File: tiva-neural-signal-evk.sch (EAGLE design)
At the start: 88 parts, among them IC1 TM4C123G, IC2 TLV70233, IC3 INA2332, IC4 OPA2320, IC5 OPA2320, IC6 INA2332, IC7 OPA2320, IC8 OPA2320, X1 USB, X2 MICROSD, Y1 16MHz, Y2 32.768kHz

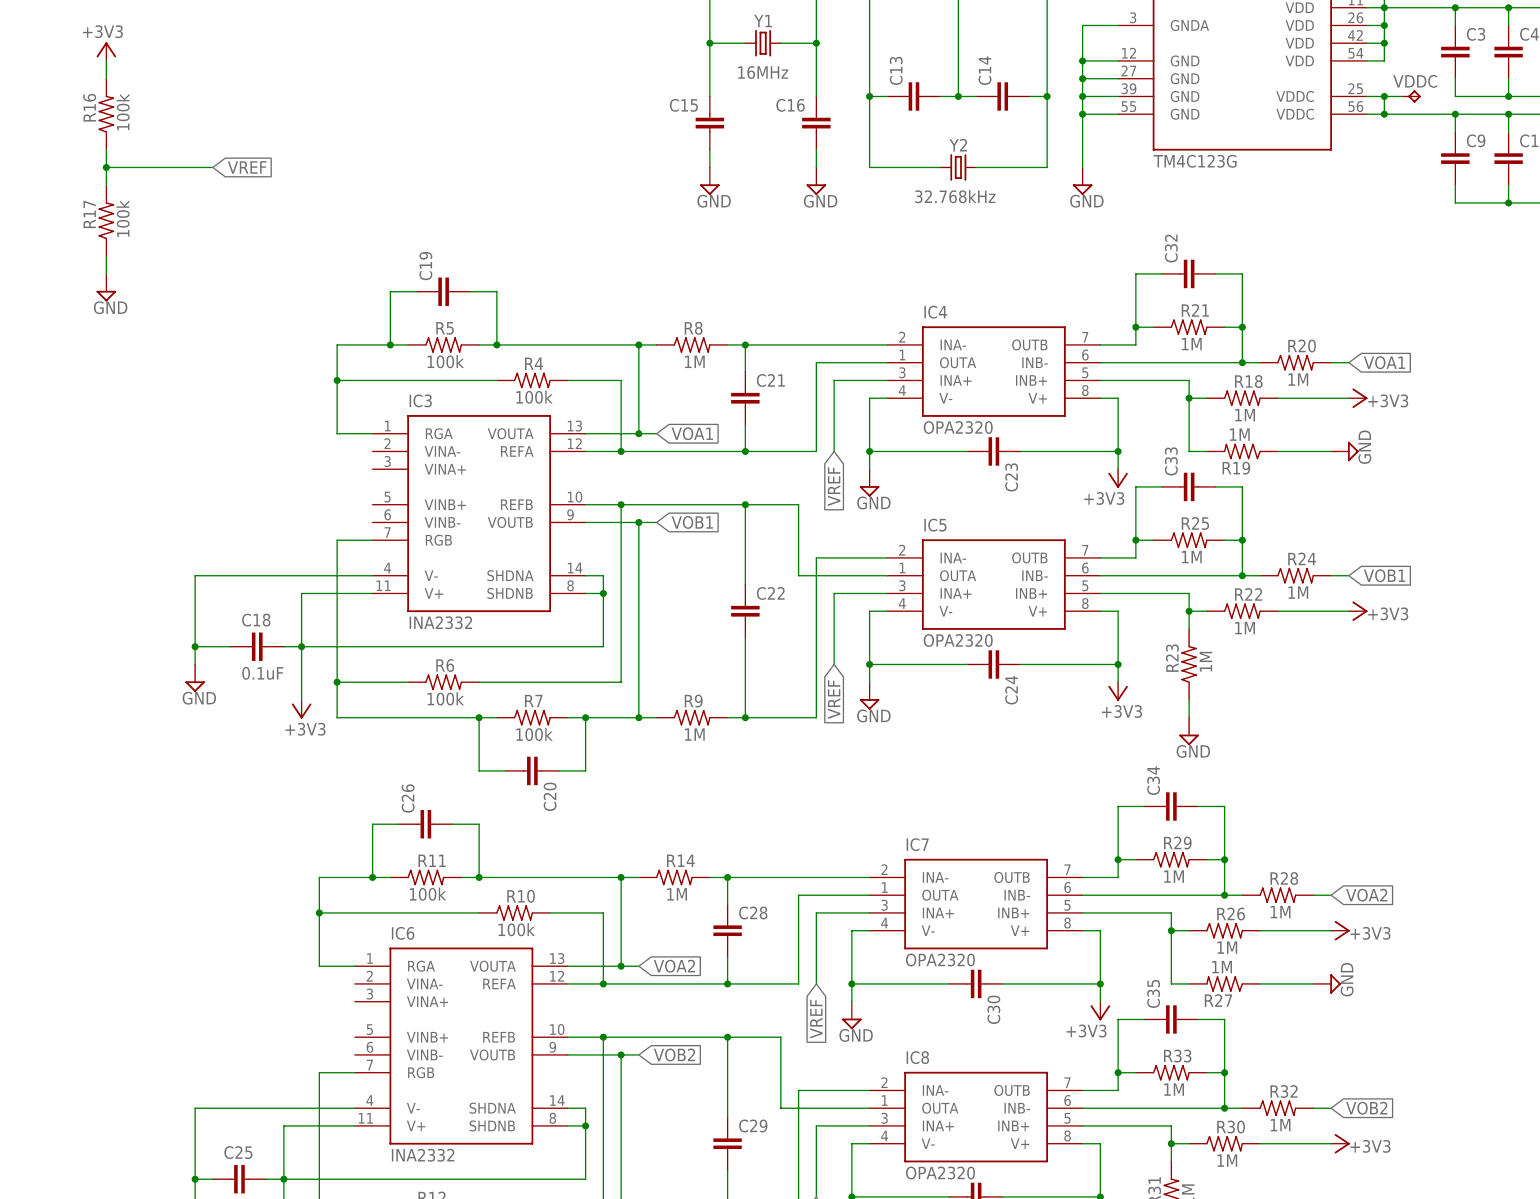
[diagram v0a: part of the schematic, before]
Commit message: laid out components
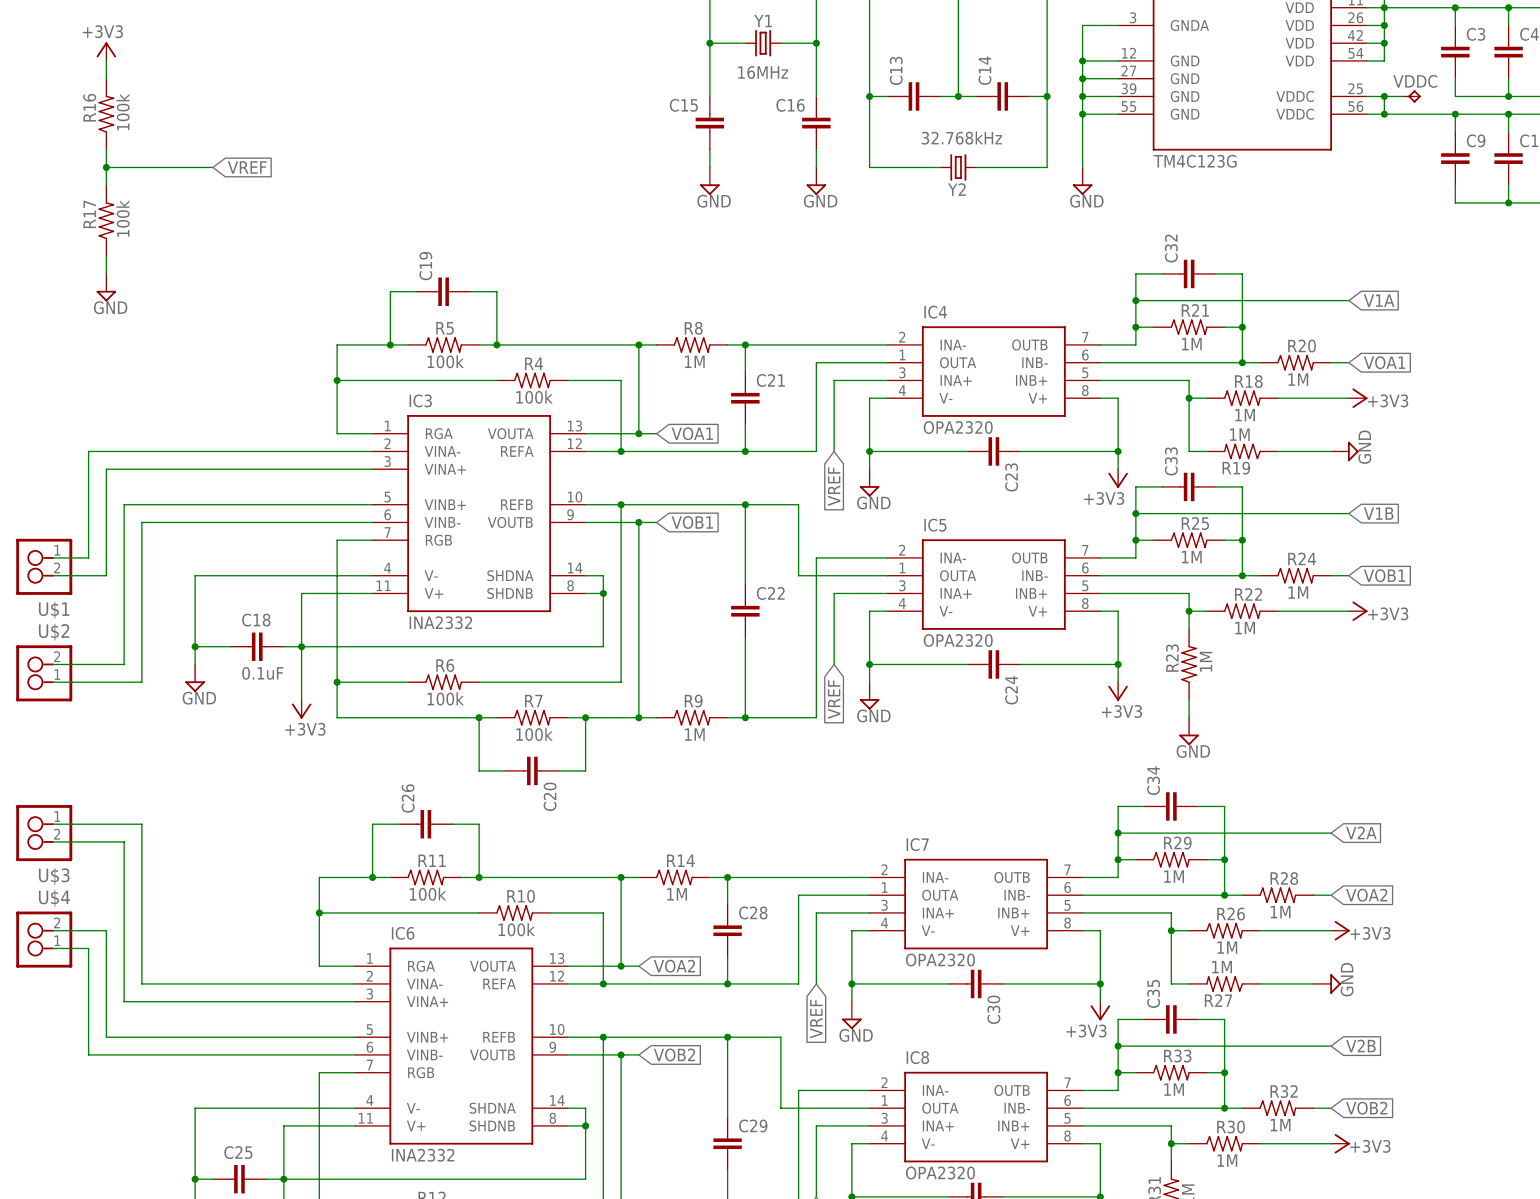
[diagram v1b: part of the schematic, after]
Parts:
- added U$1, U$2, U$3, U$4: 2_PIN_HEADERHEADER, ng:2_PIN_HEADERHEADER
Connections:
- net N$21 renamed V1A
- net N$25 renamed V1B
- net N$27 renamed V2A
- net N$30 renamed V2B
- new net N$21: IC3.VINA-, U$1.1
- new net N$25: IC3.VINA+, U$1.2
- new net N$27: IC6.VINB-, U$4.1
- new net N$30: IC6.VINB+, U$4.2
- new net N$31: IC3.VINB+, U$2.2
- new net N$32: IC3.VINB-, U$2.1
- new net N$33: IC6.VINA-, U$3.1
- new net N$34: IC6.VINA+, U$3.2
- net N$6: now also Y2.1; no longer Y2.2
- net N$8: now also Y2.2; no longer Y2.1
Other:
- moved on the sheet: Y2
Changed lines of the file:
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@@
 <part name="R33" library="rcl" deviceset="R-US_" device="R0603" value="1M"/>
 <part name="C35" library="rcl" deviceset="C-EU" device="C0603"/>
+<part name="U$1" library="ng" deviceset="2_PIN_HEADER" device="HEADER"/>
+<part name="U$2" library="ng" deviceset="2_PIN_HEADER" device="HEADER"/>
+<part name="U$3" library="ng" deviceset="2_PIN_HEADER" device="HEADER"/>
+<part name="U$4" library="ng" deviceset="2_PIN_HEADER" device="HEADER"/>
 </parts>
 <sheets>
@@
 <attribute name="VALUE" x="110.49" y="187.96" size="1.778" layer="96"/>
 </instance>
-<instance part="Y2" gate="G$1" x="142.24" y="175.26" smashed="yes">
-<attribute name="NAME" x="140.97" y="177.546" size="1.778" layer="95"/>
-<attribute name="VALUE" x="135.89" y="170.18" size="1.778" layer="96"/>
+<instance part="Y2" gate="G$1" x="142.24" y="175.26" smashed="yes" rot="R180">
+<attribute name="NAME" x="143.51" y="172.974" size="1.778" layer="95" rot="R180"/>
+<attribute name="VALUE" x="148.59" y="180.34" size="1.778" layer="96" rot="R180"/>
 </instance>
 <instance part="C13" gate="G$1" x="134.62" y="185.42" rot="R90"/>
@@
 </instance>
 <instance part="C35" gate="G$1" x="171.45" y="53.34" rot="R90"/>
+<instance part="U$1" gate="G$1" x="10.16" y="119.38" rot="R180"/>
+<instance part="U$2" gate="G$1" x="10.16" y="101.6" rot="MR0"/>
+<instance part="U$3" gate="G$1" x="10.16" y="81.28" rot="R180"/>
+<instance part="U$4" gate="G$1" x="10.16" y="63.5" rot="MR0"/>
 </instances>
 <busses>
@@
 <wire x1="154.94" y1="185.42" x2="154.94" y2="175.26" width="0.1524" layer="91"/>
 <junction x="154.94" y="185.42"/>
-<pinref part="Y2" gate="G$1" pin="2"/>
-<wire x1="154.94" y1="175.26" x2="144.78" y2="175.26" width="0.1524" layer="91"/>
+<pinref part="Y2" gate="G$1" pin="1"/>
+<wire x1="144.78" y1="175.26" x2="154.94" y2="175.26" width="0.1524" layer="91"/>
 </segment>
 </net>
@@
 <wire x1="129.54" y1="185.42" x2="129.54" y2="175.26" width="0.1524" layer="91"/>
 <junction x="129.54" y="185.42"/>
-<pinref part="Y2" gate="G$1" pin="1"/>
-<wire x1="129.54" y1="175.26" x2="139.7" y2="175.26" width="0.1524" layer="91"/>
+<pinref part="Y2" gate="G$1" pin="2"/>
+<wire x1="139.7" y1="175.26" x2="129.54" y2="175.26" width="0.1524" layer="91"/>
 </segment>
 </net>
@@
 </segment>
 </net>
-<net name="N$21" class="0">
+<net name="V1A" class="0">
 <segment>
 <pinref part="IC4" gate="G$1" pin="OUTB"/>
@@
 <pinref part="C32" gate="G$1" pin="1"/>
 <wire x1="171.45" y1="160.02" x2="167.64" y2="160.02" width="0.1524" layer="91"/>
-<wire x1="167.64" y1="160.02" x2="167.64" y2="152.4" width="0.1524" layer="91"/>
+<wire x1="167.64" y1="160.02" x2="167.64" y2="156.21" width="0.1524" layer="91"/>
 <junction x="167.64" y="152.4"/>
+<wire x1="167.64" y1="156.21" x2="167.64" y2="152.4" width="0.1524" layer="91"/>
+<wire x1="167.64" y1="156.21" x2="198.12" y2="156.21" width="0.1524" layer="91"/>
+<junction x="167.64" y="156.21"/>
+<label x="198.12" y="156.21" size="1.778" layer="95" xref="yes"/>
 </segment>
 </net>
@@
 </segment>
 </net>
-<net name="N$25" class="0">
+<net name="V1B" class="0">
 <segment>
 <wire x1="162.56" y1="119.38" x2="167.64" y2="119.38" width="0.1524" layer="91"/>
@@
 <pinref part="C33" gate="G$1" pin="1"/>
 <wire x1="171.45" y1="129.54" x2="167.64" y2="129.54" width="0.1524" layer="91"/>
-<wire x1="167.64" y1="129.54" x2="167.64" y2="121.92" width="0.1524" layer="91"/>
+<wire x1="167.64" y1="129.54" x2="167.64" y2="125.73" width="0.1524" layer="91"/>
 <junction x="167.64" y="121.92"/>
 <pinref part="IC5" gate="G$1" pin="OUTB"/>
+<wire x1="167.64" y1="125.73" x2="167.64" y2="121.92" width="0.1524" layer="91"/>
+<wire x1="167.64" y1="125.73" x2="198.12" y2="125.73" width="0.1524" layer="91"/>
+<junction x="167.64" y="125.73"/>
+<label x="198.12" y="125.73" size="1.778" layer="95" xref="yes"/>
 </segment>
 </net>
@@
 </segment>
 </net>
-<net name="N$27" class="0">
+<net name="V2A" class="0">
 <segment>
 <wire x1="160.02" y1="73.66" x2="165.1" y2="73.66" width="0.1524" layer="91"/>
@@
 <pinref part="C34" gate="G$1" pin="1"/>
 <wire x1="168.91" y1="83.82" x2="165.1" y2="83.82" width="0.1524" layer="91"/>
-<wire x1="165.1" y1="83.82" x2="165.1" y2="76.2" width="0.1524" layer="91"/>
+<wire x1="165.1" y1="83.82" x2="165.1" y2="80.01" width="0.1524" layer="91"/>
 <junction x="165.1" y="76.2"/>
 <pinref part="IC7" gate="G$1" pin="OUTB"/>
+<wire x1="165.1" y1="80.01" x2="165.1" y2="76.2" width="0.1524" layer="91"/>
+<wire x1="165.1" y1="80.01" x2="195.58" y2="80.01" width="0.1524" layer="91"/>
+<junction x="165.1" y="80.01"/>
+<label x="195.58" y="80.01" size="1.778" layer="95" xref="yes"/>
 </segment>
 </net>
@@
 </segment>
 </net>
-<net name="N$30" class="0">
+<net name="V2B" class="0">
 <segment>
 <wire x1="160.02" y1="43.18" x2="165.1" y2="43.18" width="0.1524" layer="91"/>
@@
 <pinref part="C35" gate="G$1" pin="1"/>
 <wire x1="168.91" y1="53.34" x2="165.1" y2="53.34" width="0.1524" layer="91"/>
-<wire x1="165.1" y1="53.34" x2="165.1" y2="45.72" width="0.1524" layer="91"/>
+<wire x1="165.1" y1="53.34" x2="165.1" y2="49.53" width="0.1524" layer="91"/>
 <junction x="165.1" y="45.72"/>
 <pinref part="IC8" gate="G$1" pin="OUTB"/>
-</segment>
-</net>
+<wire x1="165.1" y1="49.53" x2="165.1" y2="45.72" width="0.1524" layer="91"/>
+<wire x1="165.1" y1="49.53" x2="195.58" y2="49.53" width="0.1524" layer="91"/>
+<junction x="165.1" y="49.53"/>
+<label x="195.58" y="49.53" size="1.778" layer="95" xref="yes"/>
+</segment>
+</net>
+<net name="N$21" class="0">
+<segment>
+<pinref part="IC3" gate="G$1" pin="VINA-"/>
+<wire x1="58.42" y1="134.62" x2="17.78" y2="134.62" width="0.1524" layer="91"/>
+<wire x1="17.78" y1="134.62" x2="17.78" y2="119.38" width="0.1524" layer="91"/>
+<pinref part="U$1" gate="G$1" pin="1"/>
+<wire x1="17.78" y1="119.38" x2="12.7" y2="119.38" width="0.1524" layer="91"/>
+</segment>
+</net>
+<net name="N$25" class="0">
+<segment>
+<pinref part="IC3" gate="G$1" pin="VINA+"/>
+<wire x1="58.42" y1="132.08" x2="20.32" y2="132.08" width="0.1524" layer="91"/>
+<wire x1="20.32" y1="132.08" x2="20.32" y2="116.84" width="0.1524" layer="91"/>
+<pinref part="U$1" gate="G$1" pin="2"/>
+<wire x1="20.32" y1="116.84" x2="12.7" y2="116.84" width="0.1524" layer="91"/>
+</segment>
+</net>
+<net name="N$27" class="0">
+<segment>
+<pinref part="IC6" gate="G$1" pin="VINB-"/>
+<wire x1="55.88" y1="48.26" x2="17.78" y2="48.26" width="0.1524" layer="91"/>
+<wire x1="17.78" y1="48.26" x2="17.78" y2="63.5" width="0.1524" layer="91"/>
+<pinref part="U$4" gate="G$1" pin="1"/>
+<wire x1="17.78" y1="63.5" x2="12.7" y2="63.5" width="0.1524" layer="91"/>
+</segment>
+</net>
+<net name="N$30" class="0">
+<segment>
+<pinref part="IC6" gate="G$1" pin="VINB+"/>
+<wire x1="55.88" y1="50.8" x2="20.32" y2="50.8" width="0.1524" layer="91"/>
+<wire x1="20.32" y1="50.8" x2="20.32" y2="66.04" width="0.1524" layer="91"/>
+<pinref part="U$4" gate="G$1" pin="2"/>
+<wire x1="20.32" y1="66.04" x2="12.7" y2="66.04" width="0.1524" layer="91"/>
+</segment>
+</net>
+<net name="N$31" class="0">
+<segment>
+<pinref part="IC3" gate="G$1" pin="VINB+"/>
+<wire x1="58.42" y1="127" x2="22.86" y2="127" width="0.1524" layer="91"/>
+<wire x1="22.86" y1="127" x2="22.86" y2="104.14" width="0.1524" layer="91"/>
+<pinref part="U$2" gate="G$1" pin="2"/>
+<wire x1="22.86" y1="104.14" x2="12.7" y2="104.14" width="0.1524" layer="91"/>
+</segment>
+</net>
+<net name="N$32" class="0">
+<segment>
+<pinref part="IC3" gate="G$1" pin="VINB-"/>
+<wire x1="58.42" y1="124.46" x2="25.4" y2="124.46" width="0.1524" layer="91"/>
+<wire x1="25.4" y1="124.46" x2="25.4" y2="101.6" width="0.1524" layer="91"/>
+<pinref part="U$2" gate="G$1" pin="1"/>
+<wire x1="25.4" y1="101.6" x2="12.7" y2="101.6" width="0.1524" layer="91"/>
+</segment>
+</net>
+<net name="N$33" class="0">
+<segment>
+<pinref part="IC6" gate="G$1" pin="VINA-"/>
+<wire x1="55.88" y1="58.42" x2="25.4" y2="58.42" width="0.1524" layer="91"/>
+<wire x1="25.4" y1="58.42" x2="25.4" y2="81.28" width="0.1524" layer="91"/>
+<pinref part="U$3" gate="G$1" pin="1"/>
+<wire x1="25.4" y1="81.28" x2="12.7" y2="81.28" width="0.1524" layer="91"/>
+</segment>
+</net>
+<net name="N$34" class="0">
+<segment>
+<pinref part="IC6" gate="G$1" pin="VINA+"/>
+<wire x1="55.88" y1="55.88" x2="22.86" y2="55.88" width="0.1524" layer="91"/>
+<wire x1="22.86" y1="55.88" x2="22.86" y2="78.74" width="0.1524" layer="91"/>
+<pinref part="U$3" gate="G$1" pin="2"/>
+<wire x1="22.86" y1="78.74" x2="12.7" y2="78.74" width="0.1524" layer="91"/>
+</segment>
+</net>

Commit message: added usb and adc connections
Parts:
- removed +3V3, RESET, VBUS: TPB1,27, testpad:TPB1,27
- removed U$1, U$2, U$3, U$4: 2_PIN_HEADERHEADER, ng:2_PIN_HEADERHEADER
- added REF1, REF2, REF3, REF4, SIG1, SIG2, SIG3, SIG4: (no value), pinhead:PINHD-1X1
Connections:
- removed net N$31: IC3.VINB+, U$2.2
- removed net V1A: C32.1, IC4.OUTB, R21.1
- removed net V1B: C33.1, IC5.OUTB, R25.1
- removed net V2A: C34.1, IC7.OUTB, R29.1
- removed net V2B: C35.1, IC8.OUTB, R33.1
- new net SIG2: IC3.VINB+, SIG2.1
- new net USBDM: IC1A.PD4, X1.P$5
- new net USBDP: IC1A.PD5, X1.P$4
- net !RESET!: no longer RESET.TP
- net +3V3: no longer +3V3.TP
- net N$21: now also REF1.1; no longer U$1.1
- net N$25: now also SIG1.1; no longer U$1.2
- net N$27: now also REF4.1; no longer U$4.1
- net N$30: now also SIG4.1; no longer U$4.2
- net N$32: now also REF2.1; no longer U$2.1
- net N$33: now also REF3.1; no longer U$3.1
- net N$34: now also SIG3.1; no longer U$3.2
- net PE0: now also C35.1, IC8.OUTB, R33.1
- net PE1: now also C34.1, IC7.OUTB, R29.1
- net PE2: now also C33.1, IC5.OUTB, R25.1
- net PE3: now also C32.1, IC4.OUTB, R21.1
- net VBUS: no longer VBUS.TP

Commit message: Revert "Revert "added everything. initial routing complete with signal planes""
This reverts commit d55bffc2993c446258426b3721d1dfd936908fa6.
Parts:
- removed !HIB!, !WAKE!, VDDC: TPB1,27, testpad:TPB1,27
- added BATT, JP3: M02PTH, SparkFun-Connectors:M02PTH
- added CH1, CH2, CH3, CH4: M01NOSILK-KIT, SparkFun-Connectors:M01NOSILK-KIT
- added JP1: M05X2PTH, SparkFun-Connectors:M05X2PTH
- added JP2: (no value), SparkFun-Connectors:M07
- added JP4, JP5: (no value), SparkFun-Connectors:M05PTH
- added JP6, JP7, JP8: M021X02_NO_SILK, SparkFun-Connectors:M021X02_NO_SILK
- added LED2, LED3, LED4, LED5: (no value), led:LEDCHIP-LED0603
- added R34, R35, R36, R37: 330E, rcl:R-US_R0603
- added R38: 0E, rcl:R-US_R0603
- S1: device mor307:6MM_SWITCH6MM_SWITCH -> CEDTv82:10-XX
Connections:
- new net AGND: C18.2, C23.2, C24.2, C25.2, C30.2, C31.2, IC3.V-, IC4.V-, IC5.V-, IC6.V-, IC7.V-, IC8.V-, JP5.1, JP5.2, JP5.3, JP5.4, JP5.5, R17.1, R19.1, R23.1, R27.1, R31.1, R38.2
- new net N$31: LED2.A, R34.2
- new net N$35: LED3.A, R35.2
- new net N$36: LED4.A, R36.2
- new net N$37: LED5.A, R37.2
- new net N$38: IC2.OUT, JP6.1
- new net N$39: BATT.1, R38.1
- new net N$40: JP7.2, X2.VCC
- new net N$41: JP1.1, JP1.2, JP8.1
- net !HIB!: no longer !HIB!.TP
- net !RESET!: no longer S1.S1
- net !WAKE!: no longer !WAKE!.TP
- net +3V3: now also JP3.2, JP4.1, JP4.2, JP4.3, JP4.4, JP4.5, JP6.2, JP7.1, JP8.2, R34.1, R35.1, R36.1, R37.1; no longer IC2.OUT, X2.VCC
- net GND: now also JP1.10, JP1.9, JP2.1; no longer C18.2, C23.2, C24.2, C25.2, C30.2, C31.2, IC3.V-, IC4.V-, IC5.V-, IC6.V-, IC7.V-, IC8.V-, R17.1, R19.1, R23.1, R27.1, R31.1, S1.P1
- net PA0: now also JP2.2
- net PA1: now also JP2.3
- net PB0: now also LED2.C
- net PB1: now also LED3.C
- net PB2: now also LED4.C
- net PB3: now also LED5.C
- net PB6: now also JP1.3
- net PB7: now also JP1.8
- net PC0: now also JP2.4
- net PC1: now also JP2.5
- net PC2: now also JP2.6
- net PC3: now also JP2.7
- net PD0: now also JP1.5
- net PD1: now also JP1.4
- net PD2: now also JP1.7
- net PD3: now also JP1.6
- net PE0: now also CH4.1
- net PE1: now also CH3.1
- net PE2: now also CH2.1
- net PE3: now also CH1.1
- net PF3: now also JP3.1
- net VBUS: now also BATT.2
- net VDDC: no longer VDDC.TP
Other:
- moved on the sheet: C2, LED1, R1

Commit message: Revert "added everything. initial routing complete with signal planes"
This reverts commit afc261f9183dc80193b5e18bad7752eddb98d99b.
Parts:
- removed BATT, JP3: M02PTH, SparkFun-Connectors:M02PTH
- removed CH1, CH2, CH3, CH4: M01NOSILK-KIT, SparkFun-Connectors:M01NOSILK-KIT
- removed JP1: M05X2PTH, SparkFun-Connectors:M05X2PTH
- removed JP2: (no value), SparkFun-Connectors:M07
- removed JP4, JP5: (no value), SparkFun-Connectors:M05PTH
- removed JP6, JP7, JP8: M021X02_NO_SILK, SparkFun-Connectors:M021X02_NO_SILK
- removed LED2, LED3, LED4, LED5: (no value), led:LEDCHIP-LED0603
- removed R34, R35, R36, R37: 330E, rcl:R-US_R0603
- removed R38: 0E, rcl:R-US_R0603
- added !HIB!, !WAKE!, VDDC: TPB1,27, testpad:TPB1,27
- S1: device CEDTv82:10-XX -> mor307:6MM_SWITCH6MM_SWITCH
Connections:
- removed net AGND: C18.2, C23.2, C24.2, C25.2, C30.2, C31.2, IC3.V-, IC4.V-, IC5.V-, IC6.V-, IC7.V-, IC8.V-, JP5.1, JP5.2, JP5.3, JP5.4, JP5.5, R17.1, R19.1, R23.1, R27.1, R31.1, R38.2
- removed net N$31: LED2.A, R34.2
- removed net N$35: LED3.A, R35.2
- removed net N$36: LED4.A, R36.2
- removed net N$37: LED5.A, R37.2
- removed net N$38: IC2.OUT, JP6.1
- removed net N$39: BATT.1, R38.1
- removed net N$40: JP7.2, X2.VCC
- removed net N$41: JP1.1, JP1.2, JP8.1
- net !HIB!: now also !HIB!.TP
- net !RESET!: now also S1.S1
- net !WAKE!: now also !WAKE!.TP
- net +3V3: now also IC2.OUT, X2.VCC; no longer JP3.2, JP4.1, JP4.2, JP4.3, JP4.4, JP4.5, JP6.2, JP7.1, JP8.2, R34.1, R35.1, R36.1, R37.1
- net GND: now also C18.2, C23.2, C24.2, C25.2, C30.2, C31.2, IC3.V-, IC4.V-, IC5.V-, IC6.V-, IC7.V-, IC8.V-, R17.1, R19.1, R23.1, R27.1, R31.1, S1.P1; no longer JP1.10, JP1.9, JP2.1
- net PA0: no longer JP2.2
- net PA1: no longer JP2.3
- net PB0: no longer LED2.C
- net PB1: no longer LED3.C
- net PB2: no longer LED4.C
- net PB3: no longer LED5.C
- net PB6: no longer JP1.3
- net PB7: no longer JP1.8
- net PC0: no longer JP2.4
- net PC1: no longer JP2.5
- net PC2: no longer JP2.6
- net PC3: no longer JP2.7
- net PD0: no longer JP1.5
- net PD1: no longer JP1.4
- net PD2: no longer JP1.7
- net PD3: no longer JP1.6
- net PE0: no longer CH4.1
- net PE1: no longer CH3.1
- net PE2: no longer CH2.1
- net PE3: no longer CH1.1
- net PF3: no longer JP3.1
- net VBUS: no longer BATT.2
- net VDDC: now also VDDC.TP
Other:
- moved on the sheet: C2, LED1, R1
